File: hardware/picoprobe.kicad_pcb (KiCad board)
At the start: 2 copper layers, 24 x 41 mm, 34 parts, among them J1 Conn_01x04_Pin, J2 Conn_01x03_Pin, J3 Conn_01x03_Pin, J4 Conn_01x03_Pin, U2 74AUP1G17, U3 74AUP1G17

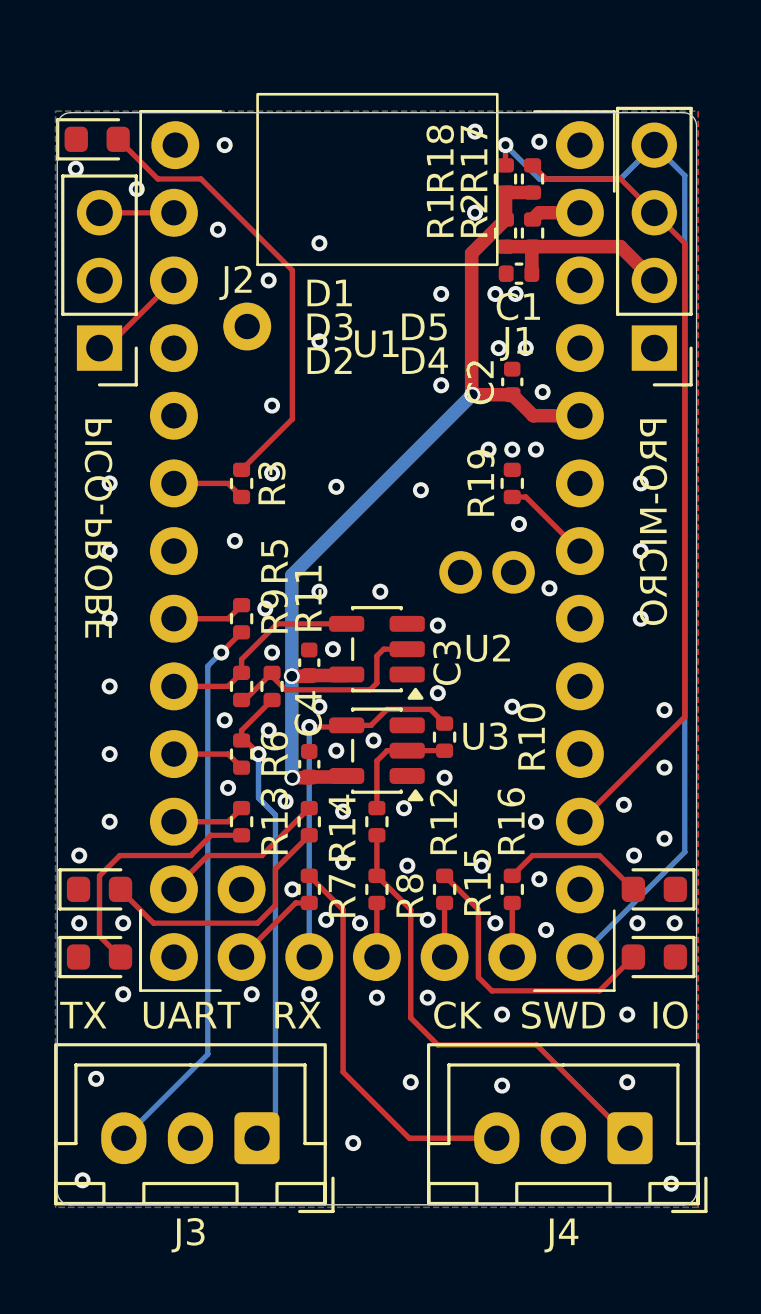
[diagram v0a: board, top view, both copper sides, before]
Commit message: Add panelization script and gerber production files
- Add make_smt_sample.py: 2x2 kikit panelization with frame, mousebites,
  tooling holes, and fiducials (panel < 10cm per side)
- Add production gerber ZIP, BOM, positions, and netlist
- Add panelized KiCad PCB files (picoprobe_panel)
- Update .gitignore to exclude KiCad backups and fabrication toolkit
  nested output

Co-Authored-By: Claude Sonnet 4.6 <noreply@anthropic.com>
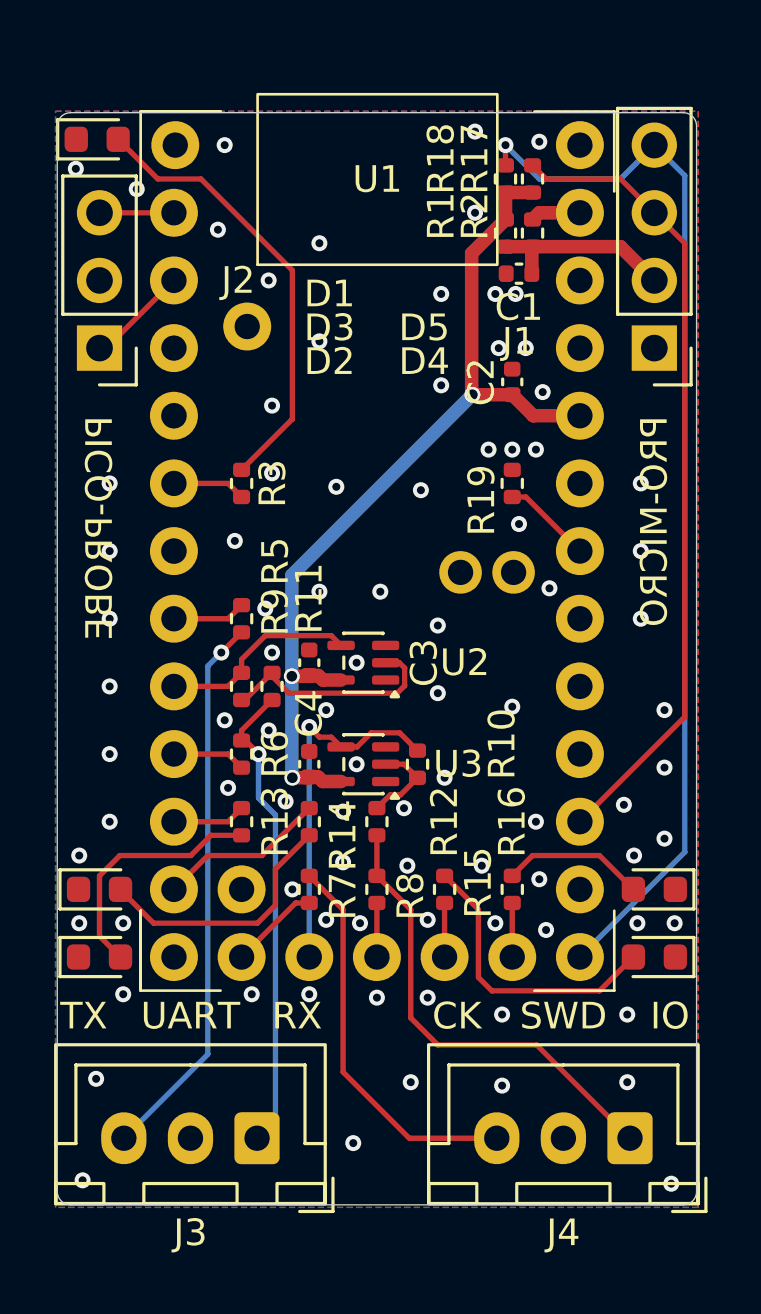
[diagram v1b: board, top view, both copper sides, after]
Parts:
- U2, U3: footprint Package_TO_SOT_SMD:SOT-23-5 -> Package_TO_SOT_SMD:SOT-353_SC-70-5
- moved R10 1.44 mm to (82.5, 64.5)
- moved U2 0.72 mm to (80.5, 60.6)
- moved U3 0.72 mm to (80.5, 64.5)
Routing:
- net Net-(R10-Pad2): track 4.47 -> 3.40 mm
- net /GPIO13: track 14.2 -> 13.5 mm
- net GND: vias 89 -> 88

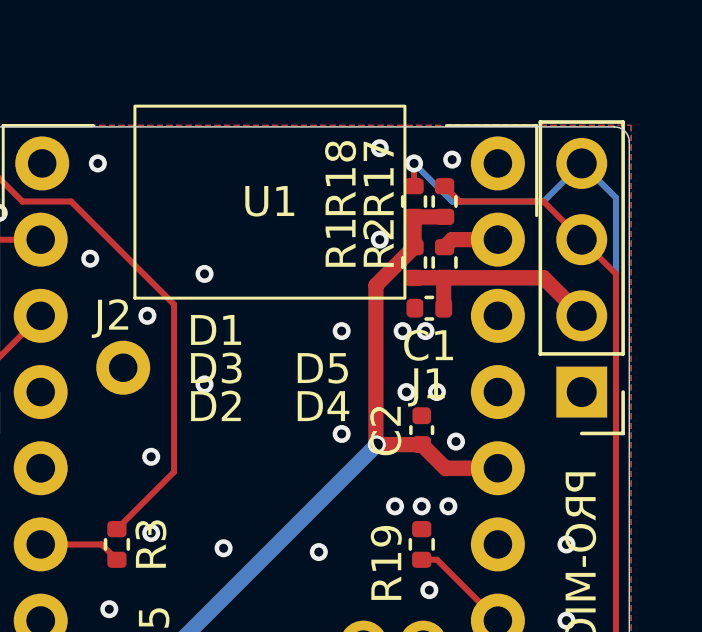
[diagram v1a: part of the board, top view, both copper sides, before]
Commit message: Update PCB layout: R18/R19 footprints to 0603, adjust component positions
Co-Authored-By: Claude Sonnet 4.6 <noreply@anthropic.com>
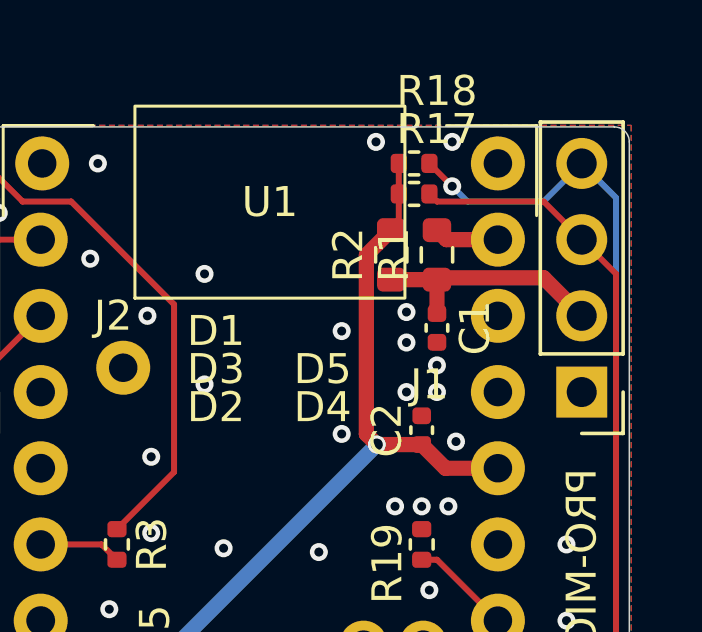
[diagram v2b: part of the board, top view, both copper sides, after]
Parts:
- R1, R2: footprint Resistor_SMD:R_0402_1005Metric -> Resistor_SMD:R_0603_1608Metric
- moved R18 1.27 mm to (85.8, 41.2), turned to 180 degrees
- moved R17 1.05 mm to (85.8, 42.2), turned to 180 degrees
- moved R2 0.80 mm to (85.1, 44.3)
- moved C1 0.70 mm to (86.6, 46.7), turned to -90 degrees
- moved R1 0.36 mm to (86.6, 44.3)
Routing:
- net /GPIO21: track 40.0 -> 38.7 mm
- net Net-(J1-Pin_2): track 7.14 -> 8.03 mm
- net +3V3: track 34.5 -> 35.4 mm

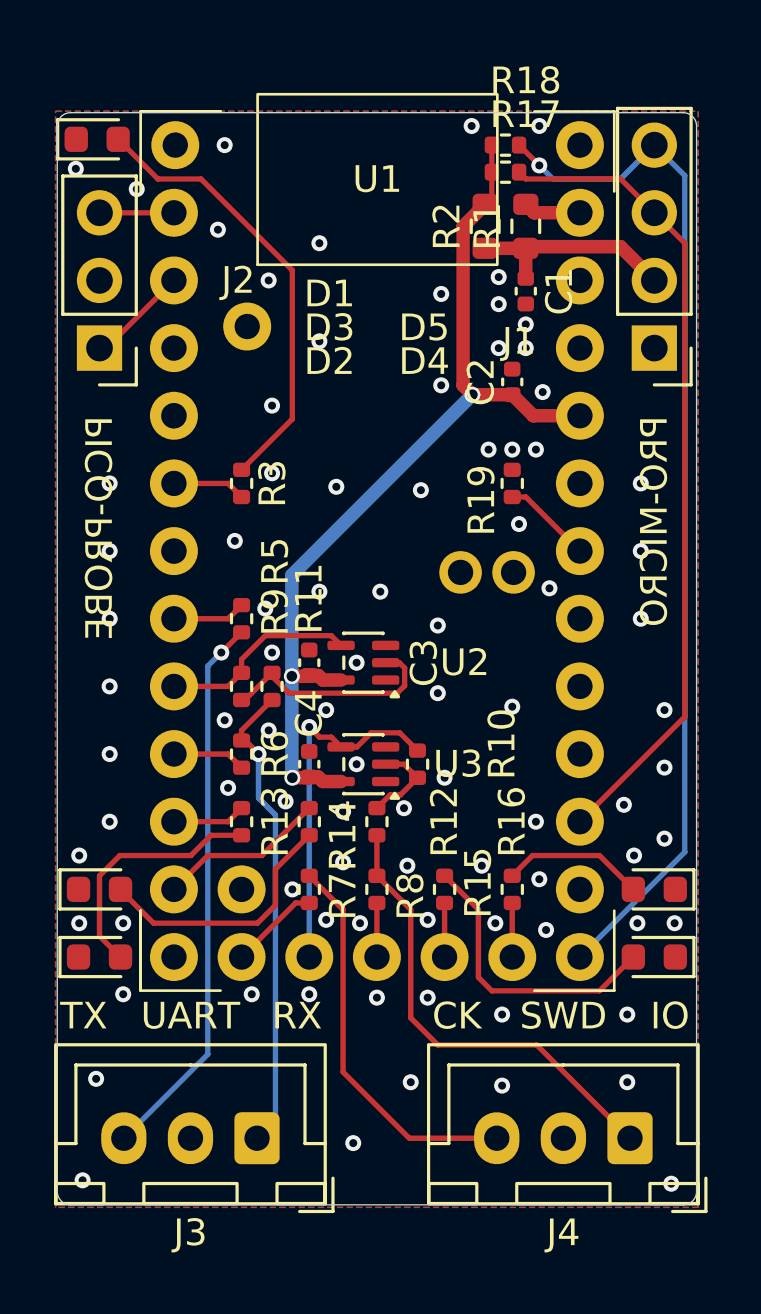
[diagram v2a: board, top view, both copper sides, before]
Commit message: Minor PCB layout tweaks
Co-Authored-By: Claude Sonnet 4.6 <noreply@anthropic.com>
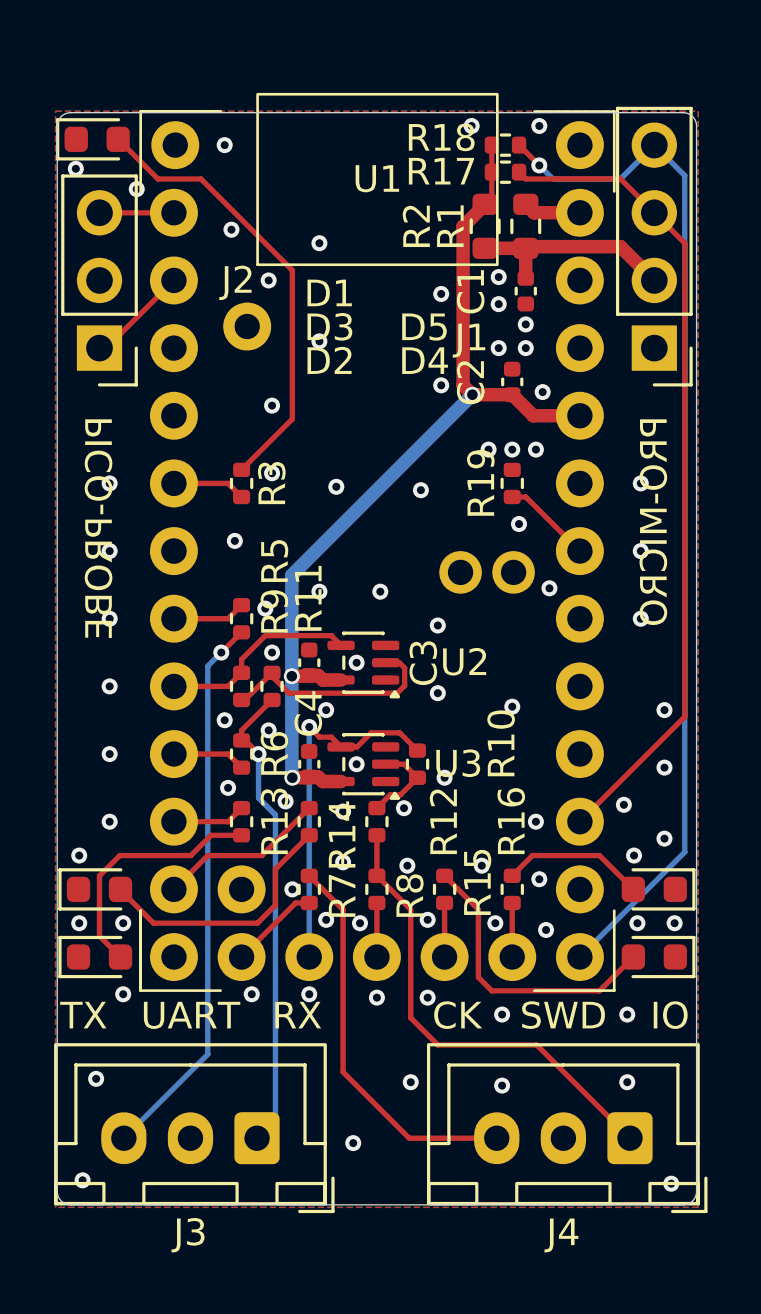
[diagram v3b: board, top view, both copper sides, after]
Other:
- board text added: "UART0"
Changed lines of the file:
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@@
 		(tags "resistor")
 		(property "Reference" "R18"
-			(at -0.762 2.413 0)
+			(at 2.413 0.254 0)
 			(layer "F.SilkS")
 			(effects
@@
 		(tags "capacitor")
 		(property "Reference" "C1"
-			(at 0 -1.27 90)
+			(at 0 2.032 90)
 			(layer "F.SilkS")
 			(effects
@@
 		(tags "resistor")
 		(property "Reference" "R17"
-			(at -0.762 2.159 0)
+			(at 2.413 0 0)
 			(layer "F.SilkS")
 			(effects
@@
 		(tags "Through hole pin header THT 1x04 2.54mm single row")
 		(property "Reference" "J1"
-			(at 5.08 0.254 180)
+			(at 6.858 0.381 180)
 			(layer "F.SilkS")
 			(effects
@@
 		(tags "resistor")
 		(property "Reference" "R2"
-			(at 0 -1.43 90)
+			(at 0 -2.54 90)
 			(layer "F.SilkS")
 			(effects
@@
 		(tags "resistor")
 		(property "Reference" "R19"
-			(at 0.635 1.143 90)
+			(at 0 1.143 90)
 			(layer "F.SilkS")
 			(effects
@@
 		(tags "capacitor")
 		(property "Reference" "C2"
-			(at 0 -1.16 90)
+			(at 0 -1.524 90)
 			(layer "F.SilkS")
 			(effects
@@
 			)
 		)
-		(attr through_hole)
+		(attr through_hole dnp)
 		(duplicate_pad_numbers_are_jumpers no)
 		(fp_line
@@
 		(tags "resistor")
 		(property "Reference" "R1"
-			(at 0 -1.43 90)
+			(at 0 -2.794 90)
 			(layer "F.SilkS")
 			(effects
@@
 		)
 	)
+	(gr_text "UART0"
+		(at 75.412 43.758 90)
+		(layer "B.SilkS")
+		(effects
+			(font
+				(size 1 1)
+				(thickness 0.1)
+			)
+			(justify mirror)
+		)
+	)
 	(segment
 		(start 86.84 67.888)
@@
 	)
 	(via
-		(at 75.031 44.393)
+		(at 75.539 44.393)
 		(size 0.6)
 		(drill 0.3)
